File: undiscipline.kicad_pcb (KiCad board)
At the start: 4 copper layers, 337.8 x 133.5 mm, 334 parts, among them J1 Conn_01x04_Male, J2 USB_B_Micro, J3 Conn_01x02_Male, J4 Conn_01x02_Male, SW1 SW_Push, SW10 SW_Push, SW11 SW_Push, SW12 SW_Push, SW13 SW_Push, SW14 SW_Push, SW15 SW_Push, SW16 SW_Push, SW17 SW_Push, SW18 SW_Push, SW19 SW_Push, SW2 SW_Push, SW20 SW_Push, SW21 SW_Push, SW22 SW_Push, SW23 SW_Push, SW24 SW_Push, SW25 SW_Push, SW26 SW_Push, SW27 SW_Push, SW28 SW_Push, SW29 SW_Push, SW3 SW_Push, SW30 SW_Push, SW31 SW_Push, SW32 SW_Push, SW33 SW_Push, SW34 SW_Push, SW35 SW_Push, SW36 SW_Push, SW37 SW_Push, SW38 SW_Push, SW39 SW_Push, SW4 SW_Push, SW40 SW_Push, SW41 SW_Push, SW42 SW_Push, SW43 SW_Push, SW44 SW_Push, SW45 SW_Push, SW46 SW_Push, SW47 SW_Push, SW48 SW_Push, SW49 SW_Push, SW5 SW_Push, SW50 SW_Push, SW51 SW_Push, SW52 SW_Push, SW53 SW_Push, SW54 SW_Push, SW55 SW_Push, SW56 SW_Push, SW57 SW_Push, SW58 SW_Push, SW59 SW_Push, SW6 SW_Push, SW60 SW_Push, SW61 SW_Push, SW62 SW_Push, SW63 SW_Push, SW64 SW_Push, SW65 SW_Push, SW66 SW_Push, SW67 SW_Push, SW68 SW_Push, SW69 SW_Push, SW7 SW_Push, SW70 SW_Push, SW71 SW_Push, SW72 SW_Push, SW73 SW_Push, SW74 SW_Push, SW75 SW_Push, SW8 SW_Push, SW9 SW_Push, U1 ATmega32A-PU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

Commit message: Move PCB references
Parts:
- removed the REF** at (99.5, 74.2)
- removed the REF** at (80.5, 74.2)
- removed the REF** at (52.0, 74.2)
- removed the REF** at (275.2, 136.0)
- removed the REF** at (256.2, 136.0)
- removed the REF** at (237.2, 136.0)
- removed the REF** at (218.2, 136.0)
- removed the REF** at (199.2, 136.0)
- removed the REF** at (180.2, 136.0)
- removed the REF** at (161.2, 136.0)
- removed the REF** at (142.2, 136.0)
- removed the REF** at (123.2, 136.0)
- removed the REF** at (104.2, 136.0)
- removed the REF** at (85.2, 136.0)
- removed the REF** at (289.5, 117.0)
- removed the REF** at (270.5, 117.0)
- removed the REF** at (251.5, 117.0)
- removed the REF** at (232.5, 117.0)
- removed the REF** at (213.5, 117.0)
- removed the REF** at (194.5, 117.0)
- removed the REF** at (175.5, 117.0)
- removed the REF** at (156.5, 117.0)
- removed the REF** at (137.5, 117.0)
- removed the REF** at (118.5, 117.0)
- removed the REF** at (99.5, 117.0)
- removed the REF** at (80.5, 117.0)
- removed the REF** at (280.0, 98.0)
- removed the REF** at (261.0, 98.0)
- removed the REF** at (242.0, 98.0)
- removed the REF** at (223.0, 98.0)
- removed the REF** at (204.0, 98.0)
- removed the REF** at (185.0, 98.0)
- removed the REF** at (166.0, 98.0)
- removed the REF** at (147.0, 98.0)
- removed the REF** at (128.0, 98.0)
- removed the REF** at (109.0, 98.0)
- removed the REF** at (90.0, 98.0)
- removed the REF** at (71.0, 98.0)
- removed the REF** at (52.0, 98.0)
- removed the REF** at (308.5, 98.0)
- removed the REF** at (313.2, 117.0)
- removed the REF** at (56.8, 117.0)
- removed the REF** at (59.1, 136.0)
- removed the REF** at (360.8, 136.0)
- removed the REF** at (341.8, 136.0)
- removed the REF** at (360.8, 117.0)
- removed the REF** at (341.8, 117.0)
- removed the REF** at (360.8, 98.0)
- removed the REF** at (341.8, 98.0)
- removed the REF** at (341.8, 159.8)
- removed the REF** at (341.8, 178.8)
- removed the REF** at (360.8, 178.8)
- removed the REF** at (322.8, 178.8)
- removed the REF** at (301.4, 155.0)
- removed the REF** at (265.8, 155.0)
- removed the REF** at (246.8, 155.0)
- removed the REF** at (227.8, 155.0)
- removed the REF** at (208.8, 155.0)
- removed the REF** at (189.8, 155.0)
- removed the REF** at (170.8, 155.0)
- removed the REF** at (151.8, 155.0)
- removed the REF** at (132.8, 155.0)
- removed the REF** at (113.8, 155.0)
- removed the REF** at (94.8, 155.0)
- removed the REF** at (306.1, 136.0)
- removed the REF** at (63.9, 155.0)
- removed the REF** at (291.9, 174.0)
- removed the REF** at (268.1, 174.0)
- removed the REF** at (125.6, 174.0)
- removed the REF** at (101.9, 174.0)
- removed the REF** at (137.5, 74.2)
- removed the REF** at (78.1, 174.0)
- removed the REF** at (54.4, 174.0)
- removed the REF** at (196.9, 174.0)
- removed the REF** at (118.5, 74.2)

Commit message: Improve GND stiching
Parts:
- moved J3 3.05 mm to (246.4, 71.1)
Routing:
- net col4: track 309.0 -> 304.7 mm
- net Net-(D78-Pad2): track 35.7 -> 38.4 mm
- net col2: track 362.4 -> 360.0 mm
- net col1: track 399.1 -> 396.7 mm
- net col0: track 419.7 -> 417.3 mm
- net SDA: track 12.1 -> 13.9 mm
- net Net-(J1-Pad4): track 75.6 -> 77.2 mm
- net Net-(J1-Pad3): track 72.7 -> 74.3 mm
- net GND: vias 3 -> 17

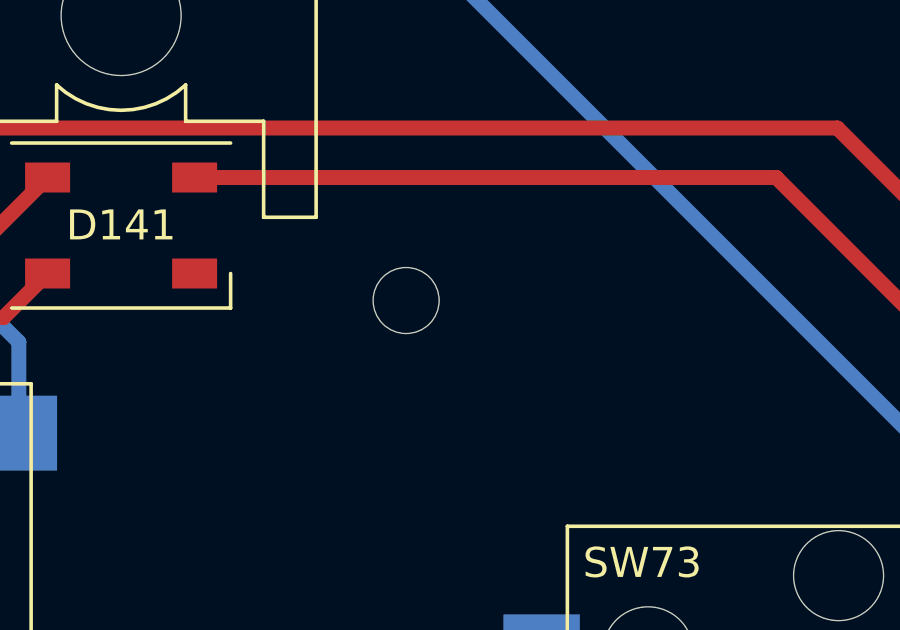
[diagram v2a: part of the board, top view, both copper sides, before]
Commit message: Change a mounting hole
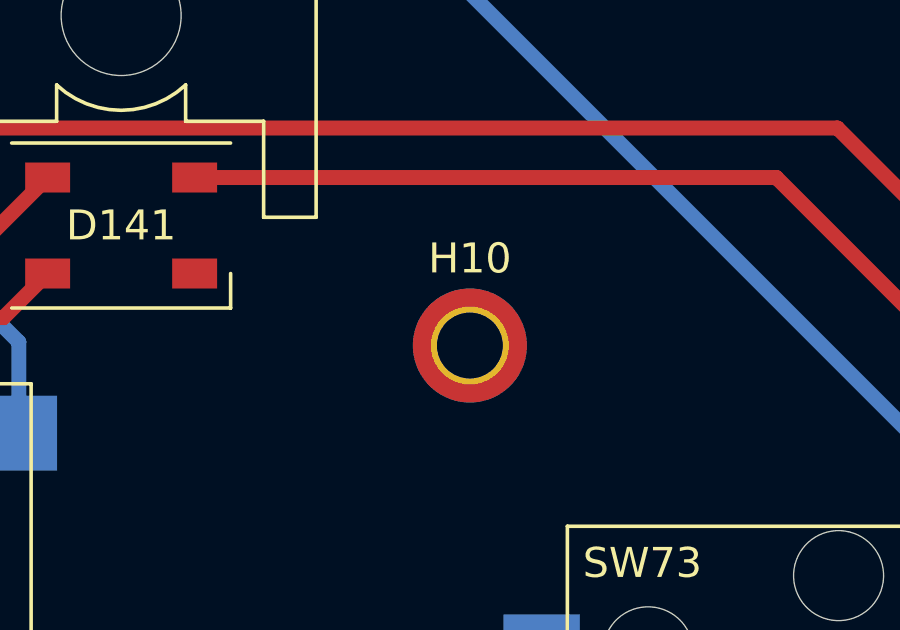
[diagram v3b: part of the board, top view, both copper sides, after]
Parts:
- removed the REF** at (310.9, 164.5)
- added H10: MountingHole_Pad, MountingHole:MountingHole_2.2mm_M2_DIN965_Pad_TopBottom, F.Cu at (313.0, 166.0)

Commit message: Add pullup resistor to D-
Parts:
- added R4: 1500, Resistor_THT:R_Axial_DIN0204_L3.6mm_D1.6mm_P5.08mm_Horizontal, F.Cu at (299.4, 63.5)
- moved R1 1.78 mm to (304.5, 72.1)
- moved R2 1.78 mm to (304.5, 69.2)
- moved R3 1.78 mm to (299.4, 66.3)
- moved C3 1.38 mm to (301.9, 75.2)
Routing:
- net +5V: track 511.1 -> 518.8 mm
- net col3: track 383.3 -> 376.3 mm
- net Net-(D77-Pad1): track 23.1 -> 29.3 mm
- net col0: track 417.3 -> 418.3 mm
- net col2: track 360.0 -> 361.0 mm
- net col1: track 396.7 -> 397.7 mm
- net boot: track 97.6 -> 98.6 mm
- net reset: track 90.9 -> 91.7 mm
- net D+: track 54.1 -> 53.3 mm
- net D-: track 57.8 -> 57.0 mm
- net Net-(D76-Pad1): track 22.1 -> 21.4 mm
